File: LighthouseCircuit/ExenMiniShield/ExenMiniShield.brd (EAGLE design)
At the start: 25.4 x 16.5 mm, 30 parts

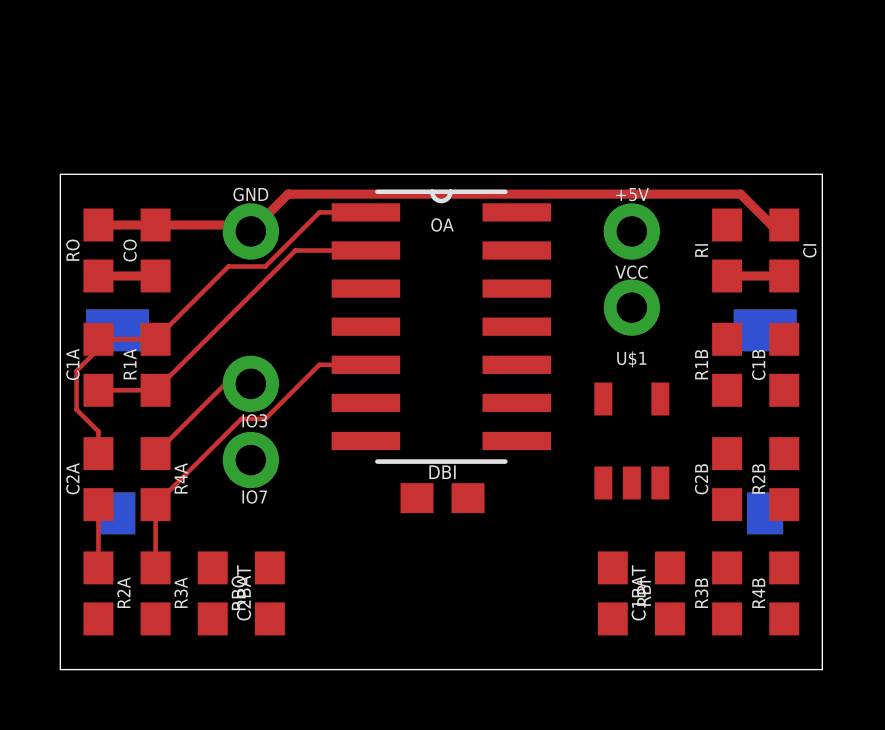
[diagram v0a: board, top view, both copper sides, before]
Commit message: Finally got the PID control ironed out. They will now smoothly follow a demo elliptical path in area of about 2 meters across and 1.5 meters in depth all on their own.
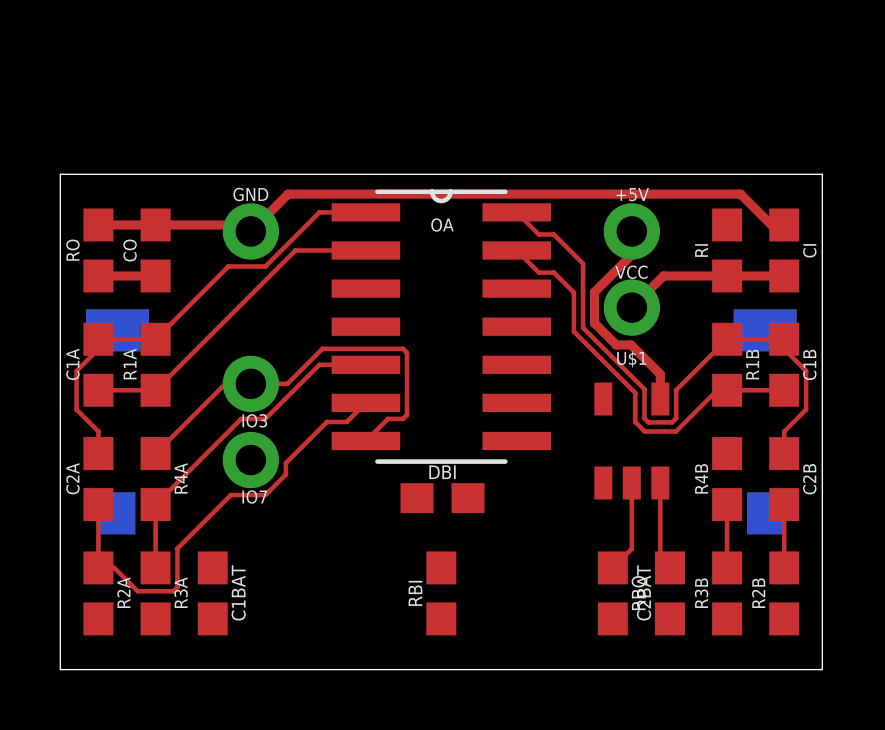
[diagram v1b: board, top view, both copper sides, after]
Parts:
- moved C2BAT 13.3 mm to (20.3, 2.54)
- moved C1BAT 13.3 mm to (5.08, 2.54)
- moved RBO 13.3 mm to (18.4, 2.54)
- moved RBI 7.62 mm to (12.7, 2.54)
- moved R4B 4.26 mm to (22.2, 6.35)
- moved R2B 3.81 mm to (24.1, 2.54)
- moved C2B 1.90 mm to (24.1, 6.35), turned to 270 degrees
- turned C1B to 90 degrees
- turned R1B to 90 degrees
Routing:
- net D1OAOUT1: track 0.00 -> 19.7 mm
- net D1IN: track 0.00 -> 13.3 mm
- net D2OA2P: track 2.11 -> 14.9 mm
- net IO3: track 4.14 -> 13.7 mm
- net +5V: track 0.00 -> 7.30 mm
- net VCC: track 1.90 -> 5.52 mm
- net N$3: track 0.00 -> 3.09 mm
- net VBAT: track 0.00 -> 2.96 mm
- net N$11: track 0.00 -> 2.11 mm
- net D1OA2P: track 0.00 -> 2.11 mm

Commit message: Modified 3D body models to use offset, direct-drive wheels because the gears were too small to be printed accurately enough to prevent binding and other movement errors that prevented accurate self-navigation. Also update the initial path to debug Zippy movement to be a figure 8 instead of a circle. Greatly improved the motion by eliminating most (though not quite all) of the overshoot and oscillations from the PID-based navigation control.
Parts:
- moved C1BAT 16.2 mm to (16.5, 14.0)
- moved RI 13.3 mm to (8.89, 14.0)
- moved CI 13.3 mm to (10.8, 14.0)
- moved RBO 12.8 mm to (24.1, 14.0)
- moved C2BAT 11.6 mm to (22.2, 14.0)
- moved RBI 11.6 mm to (14.6, 14.0)
- moved DBI 8.29 mm to (12.7, 14.0), turned to 90 degrees
- moved OA 5.71 mm to (12.7, 5.71)
- moved IO3 5.08 mm to (6.35, 4.45)
- moved IO7 5.08 mm to (6.35, 1.91)
- moved U$1 0.64 mm to (19.1, 8.26), turned to 270 degrees
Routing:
- net GND: track 23.9 -> 0.00 mm
- net D1OAOUT1: track 19.7 -> 0.00 mm
- net D2OA1OUT: track 15.1 -> 0.00 mm
- net D2OA2P: track 14.9 -> 0.00 mm
- net IO3: track 13.7 -> 0.00 mm
- net D1IN: track 13.3 -> 0.00 mm
- net D2OA2N: track 11.1 -> 0.00 mm
- net D2IN: track 10.8 -> 0.00 mm
- net +5V: track 7.30 -> 0.00 mm
- net VCC: track 5.52 -> 0.00 mm
- net N$3: track 3.09 -> 0.00 mm
- net VBAT: track 2.96 -> 0.00 mm
- net N$11: track 2.11 -> 0.00 mm
- net D1OA2P: track 2.11 -> 0.00 mm
- net LVCC: track 1.90 -> 0.00 mm

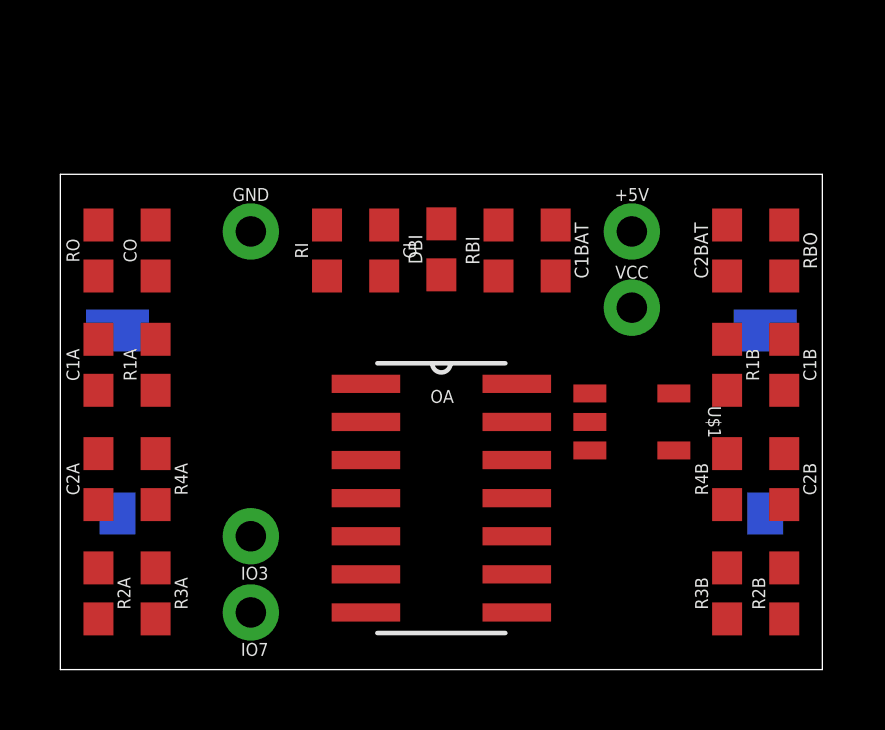
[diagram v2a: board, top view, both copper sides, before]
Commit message: Significantly stabilized the acceleration from full stop by slowing down the maximum speed. There is a physical limitation preventing them from accelerating any faster from full stop. Now that their wheels are offset, right turns cause the right wheel to lift up from the ground, creating error differences that the PID controllers are not setup to accommodate.
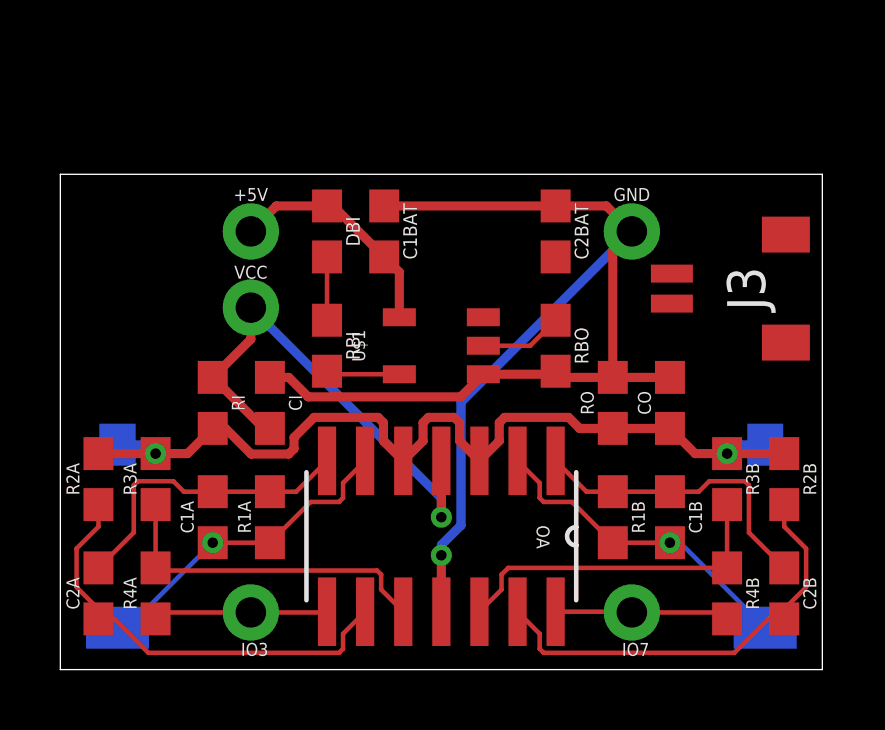
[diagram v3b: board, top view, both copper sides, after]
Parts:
- added J3: SM02B-SRSS, tinycircuits:JST_SH_2X1
- moved CO 17.9 mm to (20.3, 8.89)
- moved RO 17.9 mm to (18.4, 8.89)
- moved +5V 12.7 mm to (6.35, 14.6)
- moved GND 12.7 mm to (19.1, 14.6)
- moved IO7 12.7 mm to (19.1, 1.91)
- moved VCC 12.7 mm to (6.35, 12.1)
- moved RBO 8.25 mm to (16.5, 10.8)
- moved U$1 6.84 mm to (12.7, 10.8), turned to 90 degrees
- moved RBI 6.54 mm to (8.89, 10.8), turned to 270 degrees
- moved R1B 6.35 mm to (18.4, 5.08)
- moved C1A 6.35 mm to (5.08, 5.08)
- moved CI 6.35 mm to (6.99, 8.89)
- moved R1A 6.35 mm to (6.99, 5.08)
- moved RI 6.35 mm to (5.08, 8.89), turned to 90 degrees
- moved C1B 6.35 mm to (20.3, 5.08)
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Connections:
- net D1IN: now also OA.2; no longer OA.13
- net D1OA2P: now also OA.13; no longer OA.9
- net D1OAOUT1: now also OA.1; no longer OA.14
- net D2IN: now also OA.6; no longer OA.2
- net D2OA1OUT: now also OA.7; no longer OA.1
- net D2OA2N: now also OA.10; no longer OA.5
- net D2OA2P: now also OA.9; no longer OA.6
- net GND: now also J3.1
- net IO3: now also OA.8; no longer OA.7
- net IO7: now also OA.14; no longer OA.8
- net LVCC: now also OA.5; no longer OA.12
- net N$11: now also OA.12; no longer OA.10
- net VBAT: now also J3.2
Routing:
- net GND: track 0.00 -> 43.1 mm, vias 0 -> 1
- net LVCC: track 0.00 -> 31.4 mm, vias 0 -> 2
- net VCC: track 0.00 -> 17.0 mm, vias 0 -> 1
- net D2OA2P: track 0.00 -> 14.6 mm
- net D1OA2P: track 0.00 -> 14.6 mm
- net N$11: track 0.00 -> 11.3 mm
- net D2OA2N: track 0.00 -> 11.3 mm
- net D2IN: track 0.00 -> 10.9 mm, vias 0 -> 1
- net D1IN: track 0.00 -> 10.9 mm, vias 0 -> 1
- net D2OA1OUT: track 0.00 -> 10.3 mm
- net D1OAOUT1: track 0.00 -> 10.3 mm
- net +5V: track 0.00 -> 7.72 mm
- net IO7: track 0.00 -> 5.81 mm
- net IO3: track 0.00 -> 5.81 mm
- net N$3: track 0.00 -> 2.76 mm
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
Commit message: Reached a point where auto-drive mode is consistent and reliable.
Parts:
- removed +5V, IO3, IO7: (no value), SparkFun-Connectors:1X01_NO_SILK
- removed C1BAT: 10uF, ZippyComponentLibrary:PASSIVE-0603
- removed C2BAT: 4.7uF, ZippyComponentLibrary:PASSIVE-0603
- removed D2: PHOTODIODEBPW, ZippyComponentLibrary:BPW34_BP104_SMD
- removed U$1: BATTERYCHARGER, ZippyComponentLibrary:SOT-753
- added A1, A2, A3, A4, D0, MA01, MA02, MB01, MBO2, VIN: (no value), SparkFun-Connectors:1X01_NO_SILK
- added BC: BATTERYCHARGER, ZippyComponentLibrary:SOT-753
- added C1: 10uF, ZippyComponentLibrary:PASSIVE-0603
- added C2: 4.7uF, ZippyComponentLibrary:PASSIVE-0603
- added CB: 10μF, SparkFun-Capacitors:0603
- added D3: MBR120, tinycircuits:SOD-123FL
- added DI0, DI1: PHOTODIODEBPW, ZippyComponentLibrary:BPW34_BP104_SMD
- added MOC: A3901SEJTR-T, ZippyComponentLibrary:DFN-10_DD
- added Q1: DMP2035U, tinycircuits:SOT23
- D1: value PHOTODIODEBPW -> (none); device ZippyComponentLibrary:BPW34_BP104_SMD -> SparkFun-Connectors:1X01_NO_SILK
- GND: value SINGLE-THROUGH-HOLE -> (none); device ZippyComponentLibrary:SINGLE-THROUGH-HOLE -> SparkFun-Connectors:1X01_NO_SILK
- J3: value SM02B-SRSS -> BATTERY
- OA: value TLV2464IDM -> TLV2464IPW; device ZippyComponentLibrary:D14-M -> ZippyComponentLibrary:PW14
- moved C2B 14.9 mm to (10.2, 7.62)
- moved R2B 14.0 mm to (10.2, 7.62), flipped to the bottom
- moved J3 10.9 mm to (13.1, 17.5)
- moved R4B 9.69 mm to (14.0, 7.62)
- moved C1B 8.64 mm to (12.1, 7.62), flipped to the bottom
- moved R3B 8.35 mm to (14.0, 7.62), flipped to the bottom, turned to 270 degrees
- moved R4A 7.18 mm to (8.26, 7.62), turned to 90 degrees
- moved RI 7.10 mm to (12.1, 10.2), flipped to the bottom, turned to 0 degrees
- moved R1B 6.84 mm to (12.1, 7.62)
- moved RBO 6.63 mm to (10.2, 12.7), flipped to the bottom
- moved C2A 5.99 mm to (4.45, 7.62)
- moved R3A 5.24 mm to (8.26, 7.62), flipped to the bottom
- moved CI 5.24 mm to (12.1, 10.2), turned to 0 degrees
- moved D1 3.70 mm to (3.81, 1.27), flipped to the top, turned to 0 degrees
- moved R2A 3.42 mm to (4.45, 7.62), flipped to the bottom
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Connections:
- removed net +5V: +5V.1, C1BAT.2, DBI.1, U$1.VDD
- removed net IO3: IO3.1, OA.8, R4A.2
- removed net IO7: IO7.1, OA.14, R4B.2
- new net D0: D0.1, OA.7, R4A.2
- new net D1: D1.1, OA.8, R4B.2
- new net MA01: MBO2.1, MOC.7
- new net MA02: MB01.1, MOC.6
- new net MB01: MA02.1, MOC.10
- new net MB02: MA01.1, MOC.9
- new net N$4: A1.1, MOC.5
- new net N$5: A2.1, MOC.4
- new net N$6: A4.1, MOC.1
- new net N$7: A3.1, MOC.2
- new net VDD: BC.VDD, DBI.1, Q1.E
- new net VIN: C1.2, D3.C, Q1.C, VIN.1
- net D1IN: now also DI1.CATHODE, OA.13; no longer D2.CATHODE, OA.2
- net D1OA2P: now also OA.9; no longer OA.13
- net D1OAOUT1: now also OA.14; no longer OA.1
- net D2IN: now also DI0.CATHODE, OA.2; no longer D1.CATHODE, OA.6
- net D2OA1OUT: now also OA.1; no longer OA.7
- net D2OA2N: now also OA.5; no longer OA.10
- net D2OA2P: now also OA.6; no longer OA.9
- net GND: now also BC.VSS, C1.1, C2.1, CB.1, MOC.11, MOC.3; no longer C1BAT.1, C2BAT.1, U$1.VSS
- net LVCC: now also DI0.ANODE, DI1.ANODE, OA.12; no longer D1.ANODE, D2.ANODE, OA.5
- net N$11: now also OA.10; no longer OA.12
- net N$2: now also BC.STAT; no longer U$1.STAT
- net N$3: now also BC.PROG; no longer U$1.PROG
- net VBAT: now also BC.VBAT, C2.2, CB.2, D3.A, MOC.8, Q1.B; no longer C2BAT.2, U$1.VBAT
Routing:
- net GND: track 43.1 -> 9.14 mm, vias 1 -> 11
- net VBAT: track 0.00 -> 24.2 mm, vias 0 -> 1
- net LVCC: track 31.4 -> 48.7 mm, vias 2 -> 3
- net D1: track 0.00 -> 16.3 mm
- net D0: track 0.00 -> 14.8 mm
- net MA01: track 0.00 -> 12.6 mm
- net MB01: track 0.00 -> 11.9 mm
- net N$6: track 0.00 -> 11.8 mm
- net MB02: track 0.00 -> 11.1 mm
- net N$7: track 0.00 -> 10.0 mm
- net MA02: track 0.00 -> 9.86 mm
- net VIN: track 0.00 -> 9.85 mm, vias 0 -> 1
- net N$5: track 0.00 -> 8.48 mm
- net D2OA2P: track 14.6 -> 6.68 mm, vias 0 -> 1
- net D1OA2P: track 14.6 -> 6.83 mm, vias 0 -> 1
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- added copper zone on layer 16, net GND
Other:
- board size 25.4 x 16.5 mm -> 20.3 x 20.3 mm
- board text removed: "Designed, Manufactured, and Assembled by Kyle Davis"
